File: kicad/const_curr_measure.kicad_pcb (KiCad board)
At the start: 4 copper layers, 160 x 100 mm, 103 parts, among them IC1 XTR110AG, J1 Conn_02x02_Counter_Clockwise, J10 1-726386-2, J11 1-726386-2, J12 09061152911, J13 Conn_01x04, J2 1-726386-2, J3 Conn_01x06, J4 1-726386-2, J5 Conn_01x03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

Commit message: * most pcb routing
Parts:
- removed P1: Power, Socket_Arduino_Uno:Socket_Strip_Arduino_1x08
- removed P2: Analog, Socket_Arduino_Uno:Socket_Strip_Arduino_1x06
- removed P3: Digital, Socket_Arduino_Uno:Socket_Strip_Arduino_1x10
- removed P4: Digital, Socket_Arduino_Uno:Socket_Strip_Arduino_1x08
- removed P5, P6, P7, P8: CONN_01X01, Socket_Arduino_Uno:Arduino_1pin
- added A1: Arduino_Nano_v3.x, Module:Arduino_Nano, F.Cu at (126.4, 63.9)
- added C10: 100nF, Capacitor_THT:C_Rect_L7.2mm_W3.0mm_P5.00mm_FKS2_FKP2_MKS2_MKP2, F.Cu at (130.5, 111.9)
- added C8: 100nF, Capacitor_THT:C_Rect_L7.2mm_W3.0mm_P5.00mm_FKS2_FKP2_MKS2_MKP2, F.Cu at (121.3, 109.4)
- added RV1: 10k, Potentiometer_THT:Potentiometer_Piher_PT-6-V_Vertical, F.Cu at (125.4, 125.4)
- added TP38: 5V ref, TestPoint:TestPoint_THTPad_D2.5mm_Drill1.2mm, F.Cu at (126.4, 114.7)
- added U3: REF02CP, Package_DIP:DIP-8_W7.62mm_LongPads, F.Cu at (115.0, 113.0)
- added U4: MCP3202, Package_DIP:DIP-8_W7.62mm_LongPads, F.Cu at (133.8, 118.0)
- moved R8 60.7 mm to (138.6, 33.0), turned to 0 degrees
- moved TP35 50.0 mm to (148.5, 83.7)
- moved J3 49.3 mm to (107.1, 61.9), turned to 0 degrees
- moved TP36 47.7 mm to (121.3, 72.3)
- moved R18 47.4 mm to (161.5, 59.1)
- moved D4 45.0 mm to (128.4, 143.4), turned to 180 degrees
- moved TP34 43.8 mm to (117.0, 67.2)
- moved TP37 41.2 mm to (121.3, 81.7)
- moved R19 37.3 mm to (154.6, 56.3)
- moved TP9 35.7 mm to (133.8, 127.2)
- moved R20 30.7 mm to (148.5, 88.3), turned to 270 degrees
- moved D1 30.3 mm to (154.6, 116.5), turned to 180 degrees
- moved TP33 29.2 mm to (117.0, 77.1)
- moved TP4 26.2 mm to (121.3, 100.3)
- moved D3 22.7 mm to (154.6, 113.0), turned to 180 degrees
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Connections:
- net ARDUINO_A0 renamed ADC1
- net ARDUINO_A1 renamed ADC0
- net SPI_CS renamed DAC_CS
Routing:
- net +12V: track 304.7 -> 390.7 mm
- net ADC1: track 85.2 -> 24.7 mm
- net +5V: track 477.5 -> 421.1 mm, vias 2 -> 4
- net DAC_CS: track 70.2 -> 24.5 mm, vias 0 -> 2
- net DAC_SHDN: track 70.0 -> 25.6 mm, vias 0 -> 3
- net GND: track 240.9 -> 285.1 mm, vias 37 -> 38
- net ADC_CS: track 0.00 -> 42.9 mm
- net ADC0: track 72.0 -> 41.6 mm
- net RANGE_UP: track 29.1 -> 57.8 mm
- net +5F: track 0.00 -> 26.2 mm
- net TEMP_SENS_OW: track 23.9 -> 47.2 mm
- net ROT_POT_B: track 10.3 -> 30.5 mm
- net RANGE_DOWN: track 27.8 -> 46.2 mm, vias 0 -> 1
- net SPI_MOSI: track 80.4 -> 62.3 mm, vias 0 -> 1
- net SPI_MISO: track 0.00 -> 17.0 mm
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- removed copper zone on B.Cu, net GND

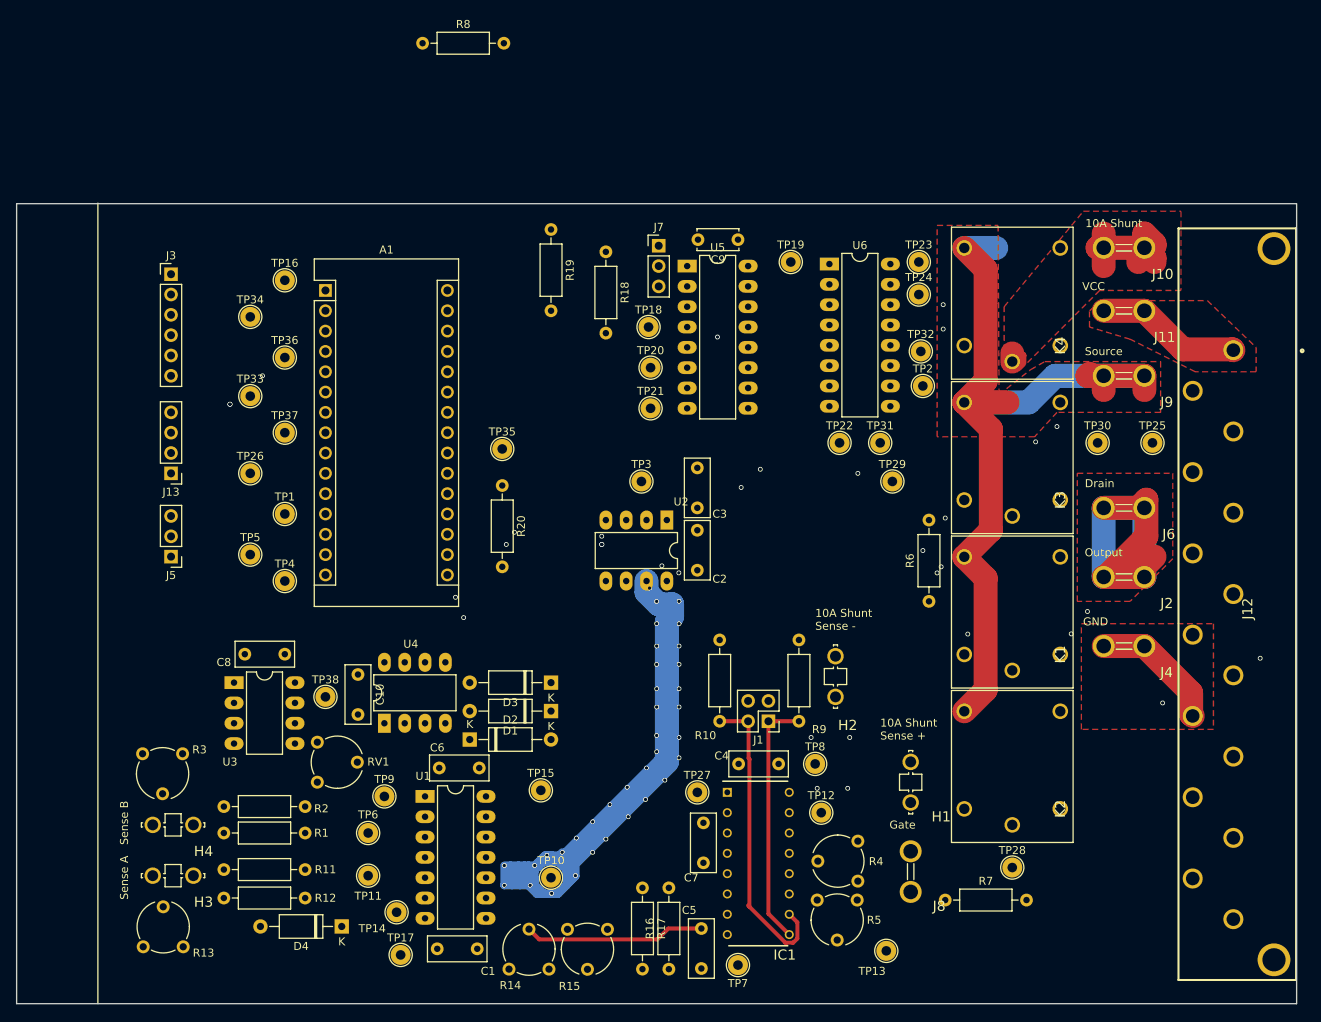
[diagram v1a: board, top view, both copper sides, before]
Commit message: * nearly finished pcb, changed front pcb connector to one big * added output enable switch net
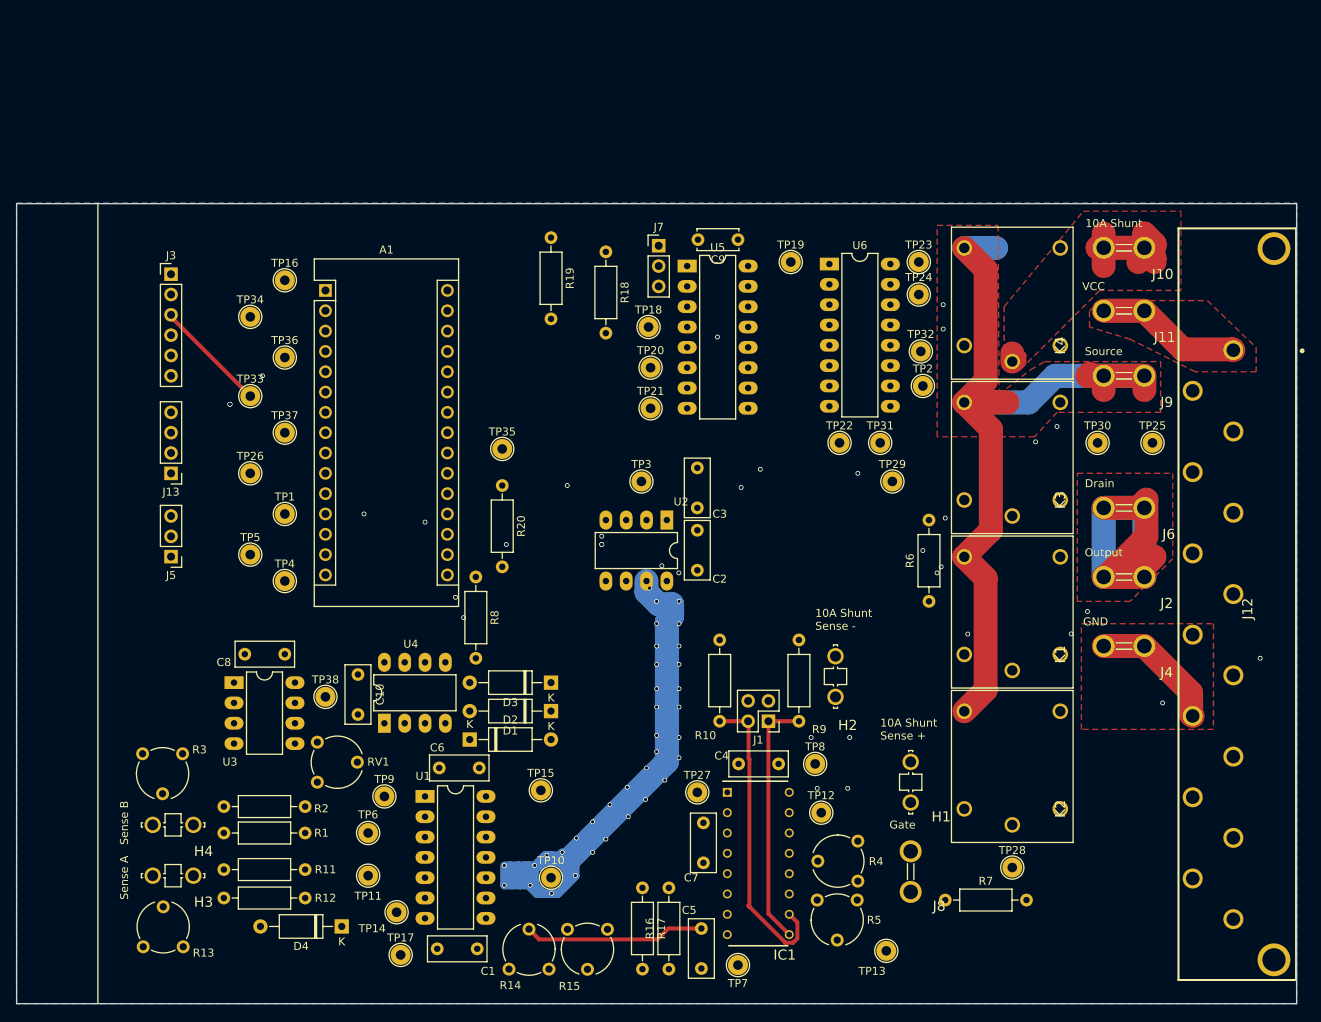
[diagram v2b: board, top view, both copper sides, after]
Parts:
- moved R8 67.0 mm to (145.2, 99.7), turned to 270 degrees
- moved R19 1.02 mm to (154.6, 57.3)
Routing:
- net DAC_SHDN: track 25.6 -> 54.2 mm, vias 3 -> 4
- net DAC_CS: track 24.5 -> 52.6 mm, vias 2 -> 3
- net ROT_POT_A: track 9.61 -> 23.9 mm
- net ADC0: track 41.6 -> 49.2 mm
- net SCL: track 79.2 -> 80.4 mm
- net +5V: track 421.1 -> 422.2 mm
- added copper zone on B.Cu, net GND

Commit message: * first revision will order this version
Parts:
- J13: value Conn_01x04 -> Conn_01x05; footprint Connector_PinHeader_2.54mm:PinHeader_1x04_P2.54mm_Vertical -> Connector_PinHeader_2.54mm:PinHeader_1x05_P2.54mm_Vertical
- J3: value Conn_01x06 -> Conn_01x12; footprint Connector_PinHeader_2.54mm:PinHeader_1x06_P2.54mm_Vertical -> Connector_PinHeader_2.54mm:PinHeader_1x12_P2.54mm_Vertical
- moved J13 126.2 mm to (226.7, 126.9), turned to 0 degrees
- moved J3 26.4 mm to (107.1, 88.3), turned to 180 degrees
- moved J5 3.30 mm to (107.1, 100.5)
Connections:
- A1 pad 19: Net-(A1-Pad19) -> OUTPUT_ENABLE
- J13 pad 1: GND -> Net-(J12-Pad11)
- J13 pad 2: +5V -> Net-(J12-Pad12)
- J13 pad 3: SDA -> Net-(J12-Pad13)
- J13 pad 4: SCL -> Net-(J12-Pad14)
- J3 pad 1: Rot_Enc_But -> GND
- J3 pad 2: ROT_POT_B -> +5V
- J3 pad 3: ROT_POT_A -> SDA
- J3 pad 4: RANGE_UP -> SCL
- J3 pad 5: RANGE_DOWN -> Rot_Enc_But
- J3 pad 6: GND -> ROT_POT_B
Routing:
- net OUTPUT_ENABLE: track 0.00 -> 48.5 mm
- net Rot_Enc_But: track 43.6 -> 21.8 mm
- net RANGE_UP: track 57.8 -> 41.2 mm
- net Net-(J12-Pad15): track 0.00 -> 15.4 mm
- net Net-(J12-Pad11): track 0.00 -> 15.1 mm
- net Net-(J12-Pad13): track 0.00 -> 13.3 mm
- net Net-(J12-Pad14): track 0.00 -> 9.28 mm
- net Net-(J12-Pad12): track 0.00 -> 8.98 mm
- net ROT_POT_B: track 30.5 -> 25.6 mm
- net +5V: track 422.2 -> 425.8 mm
- net ROT_POT_A: track 23.9 -> 21.2 mm
- net RANGE_DOWN: track 46.2 -> 47.9 mm
- net SDA: track 85.7 -> 87.2 mm
- net TEMP_SENS_OW: track 47.2 -> 48.6 mm
- net SCL: track 80.4 -> 81.0 mm

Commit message: * addded Ibom * added normal bom
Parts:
- TP1: value DAC_SHDN -> 1018.68
- TP10: value DAC_OUT -> 1018.68
- TP11: value SENSE+VDIV -> 1018.68
- TP12: value VREF_O -> 1018.68
- TP13: value VREF_ADJ -> 1018.68
- TP14: value ARD_A0 -> 1018.68
- TP15: value GND -> 1018.68
- TP16: value 5V -> 1018.68
- TP17: value DAC_OUT_FULL_SWING -> 1018.68
- TP18: value 20_EN -> 1018.68
- TP19: value 100_EN -> 1018.68
- TP2: value EN_ADD_03 -> 1018.68
- TP20: value 1000_EN -> 1018.68
- TP21: value 10000_EN -> 1018.68
- TP22: value 20_EN_Rel -> 1018.68
- TP23: value 100_EN_Rel -> 1018.68
- TP24: value 1000_EN_Rel -> 1018.68
- TP25: value 10000_EN_Rel -> 1018.68
- TP26: value TMP_S_OW -> 1018.68
- TP27: value 20mA_SHN -> 1018.68
- TP28: value 100mA_SHN -> 1018.68
- TP29: value 1000mA_SHN -> 1018.68
- TP3: value SPI_CS -> 1018.68
- TP30: value 10000mA_SHN -> 1018.68
- TP31: value EN_ADD_01 -> 1018.68
- TP32: value EN_ADD_02 -> 1018.68
- TP33: value ROT_POT_A -> 1018.68
- TP34: value ROT_POT_B -> 1018.68
- TP35: value Range_Down -> 1018.68
- TP36: value Range_up -> 1018.68
- TP37: value Rot_Enc_Button -> 1018.68
- TP38: value 5V ref -> 1018.68
- TP4: value SPI_SCK -> 1018.68
- TP5: value SPI_MOSI -> 1018.68
- TP6: value SENSE-VDIV -> 1018.68
- TP7: value SPAN_ADJ -> 1018.68
- TP8: value SRC_RES -> 1018.68
- TP9: value ARD_A1 -> 1018.68
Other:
- board text added: "5V"
- board text added: "OUT_EN"
- board text added: "RNG_D"
- board text added: "RNG_U"
- board text added: "ROT_A"
- board text added: "ROT_B"
- board text added: "ROT_BUT"
- board text added: "SCL"
- board text added: "SDA"

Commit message: current working changes for revision 0.2
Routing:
- net ADC1: track 24.7 -> 27.3 mm
